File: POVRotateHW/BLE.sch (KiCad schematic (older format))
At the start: 3 parts

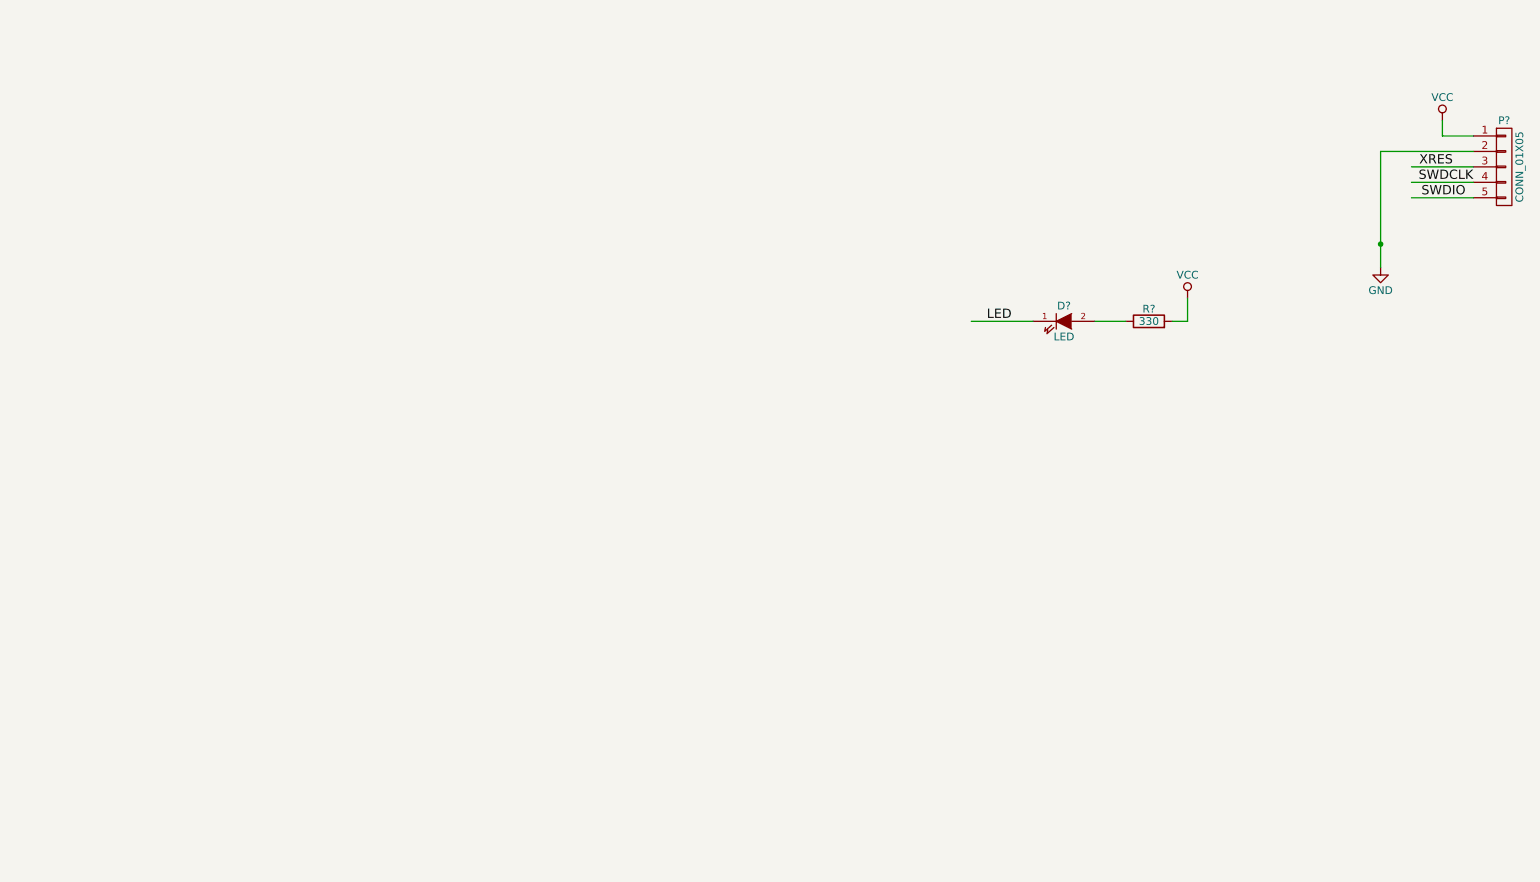
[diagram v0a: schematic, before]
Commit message: Started working on the schematic for the POV Rotate board.
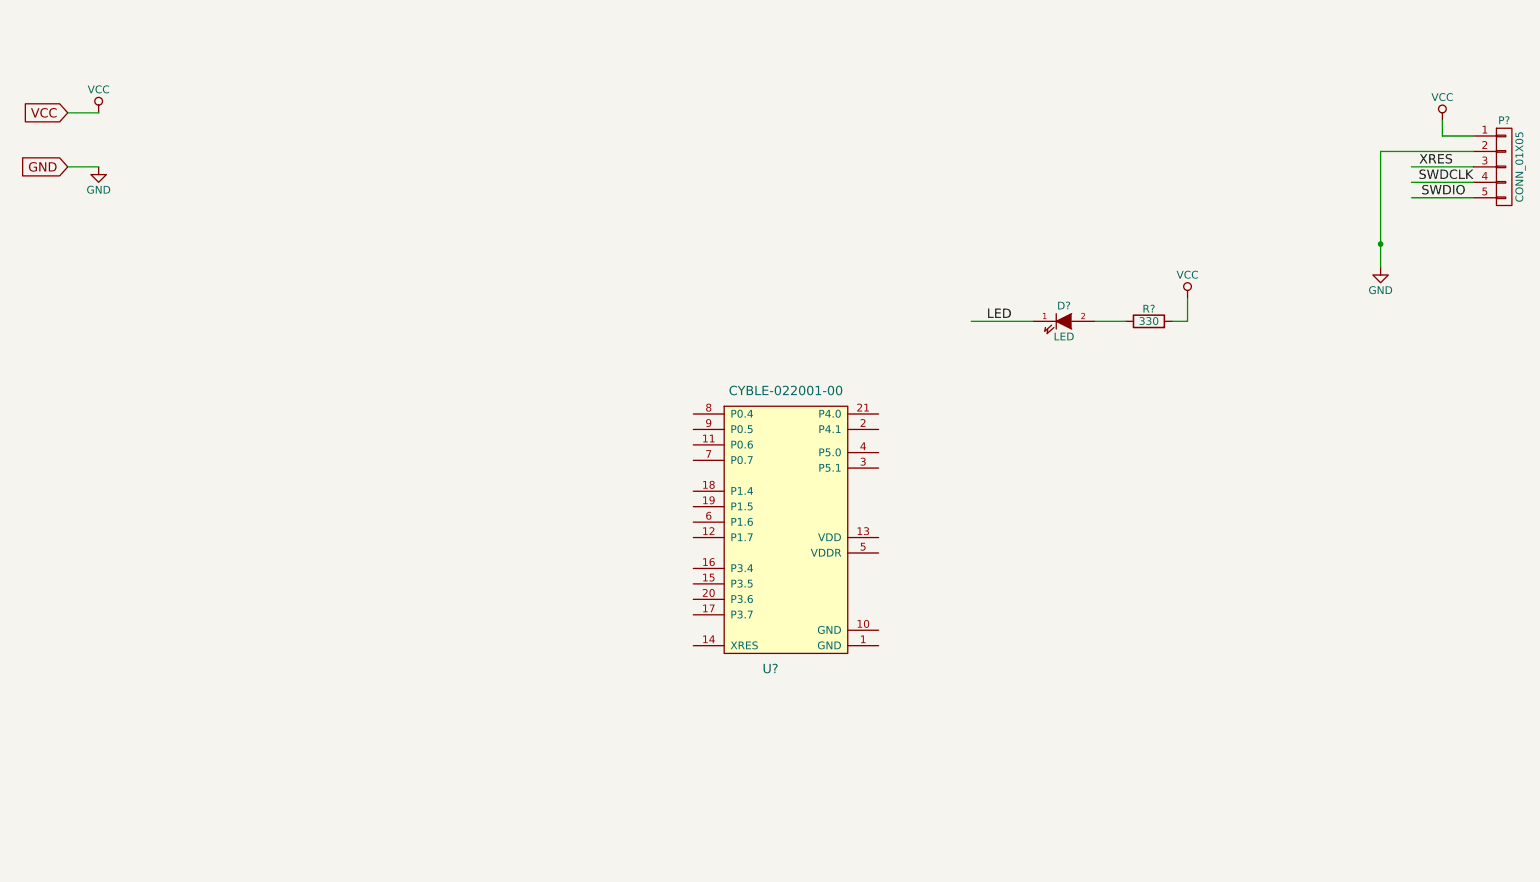
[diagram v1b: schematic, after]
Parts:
- added U?: CYBLE-022001-00, symbol CYBLE-022001-00
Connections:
- wire segments 11 -> 13
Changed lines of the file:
@@
 Text Label 10400 1700 2    60   ~ 0
 SWDIO
+$Comp
+L CYBLE-022001-00 U?
+U 1 1 5812CAAC
+P 6000 3750
+F 0 "U?" H 5900 2750 60  0000 C CNN
+F 1 "CYBLE-022001-00" H 6000 4550 60  0000 C CNN
+F 2 "" H 6000 4250 60  0001 C CNN
+F 3 "" H 6000 4250 60  0001 C CNN
+	1    6000 3750
+	1    0    0    -1
+$EndComp
+Text GLabel 1350 1150 0    60   Input ~ 0
+VCC
+Text GLabel 1350 1500 0    60   Input ~ 0
+GND
+$Comp
+L GND #PWR?
+U 1 1 581265FE
+P 1550 1500
+F 0 "#PWR?" H 1550 1250 50  0001 C CNN
+F 1 "GND" H 1550 1350 50  0000 C CNN
+F 2 "" H 1550 1500 50  0000 C CNN
+F 3 "" H 1550 1500 50  0000 C CNN
+	1    1550 1500
+	1    0    0    -1
+$EndComp
+$Comp
+L VCC #PWR?
+U 1 1 58126615
+P 1550 1150
+F 0 "#PWR?" H 1550 1000 50  0001 C CNN
+F 1 "VCC" H 1550 1300 50  0000 C CNN
+F 2 "" H 1550 1150 50  0000 C CNN
+F 3 "" H 1550 1150 50  0000 C CNN
+	1    1550 1150
+	1    0    0    -1
+$EndComp
+Wire Wire Line
+	1550 1500 1350 1500
+Wire Wire Line
+	1550 1150 1350 1150
 $EndSCHEMATC

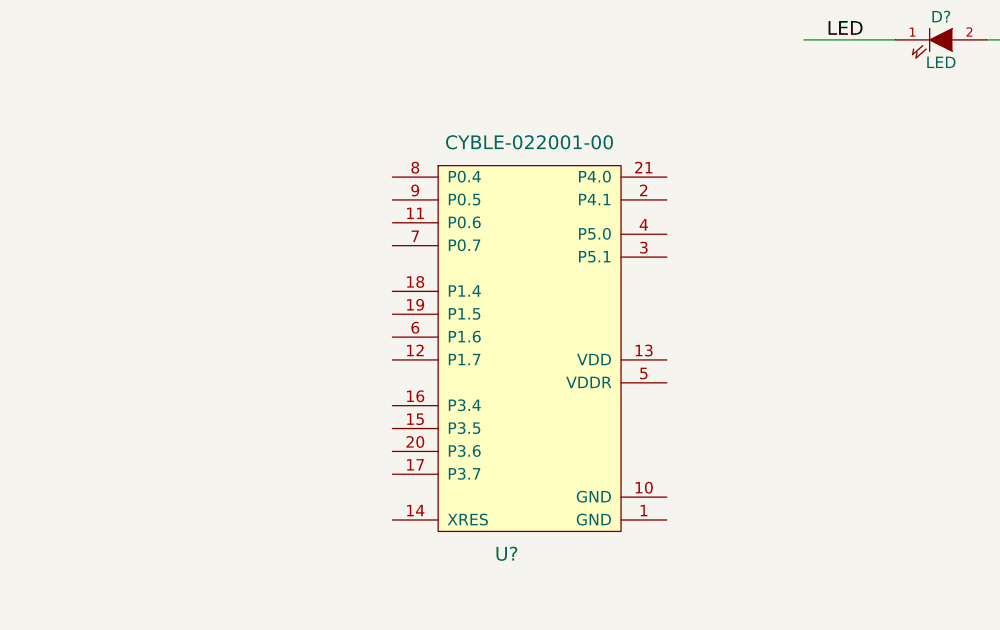
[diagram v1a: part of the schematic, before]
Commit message: Connected some pins up.
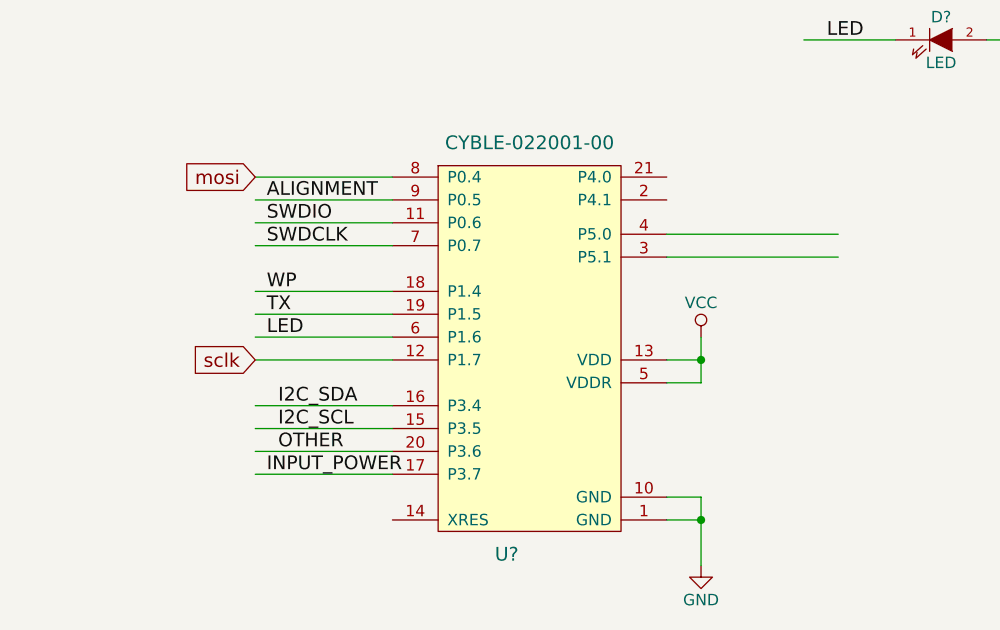
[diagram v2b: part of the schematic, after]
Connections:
- net labels added: ALIGNMENT, I2C_SCL, I2C_SDA, INPUT_POWER, OTHER, TX, WP, mosi, sclk
- wire segments 13 -> 33
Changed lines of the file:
@@
 	1    0    0    -1
 $EndComp
-Wire Wire Line
-	8500 2500 8600 2500
-Wire Wire Line
-	8600 2500 8600 2350
-Wire Wire Line
-	8000 2500 8200 2500
 $Comp
 L CONN_01X05 P?
@@
 	1    0    0    -1
 $EndComp
-Wire Wire Line
-	7600 2500 7200 2500
 Text Label 7300 2500 0    60   ~ 0
 LED
-Wire Wire Line
-	10250 1200 10250 1300
-Wire Wire Line
-	10250 1300 10450 1300
-Wire Wire Line
-	9850 1400 10450 1400
-Wire Wire Line
-	10450 1500 10050 1500
-Wire Wire Line
-	10450 1600 10050 1600
-Wire Wire Line
-	10450 1700 10050 1700
-Wire Wire Line
-	9850 1400 9850 2150
 Text Label 10100 1500 0    60   ~ 0
 XRES
-Connection ~ 9850 2000
 Text Label 10450 1600 2    60   ~ 0
 SWDCLK
@@
 	1    0    0    -1
 $EndComp
+Text GLabel 4800 3100 0    60   Input ~ 0
+mosi
+Text GLabel 4800 3900 0    60   Input ~ 0
+sclk
+Text Label 4850 3300 0    60   ~ 0
+SWDIO
+Text Label 4850 3400 0    60   ~ 0
+SWDCLK
+Text Label 4850 3800 0    60   ~ 0
+LED
+Text Label 4850 3200 0    60   ~ 0
+ALIGNMENT
+Text Label 4900 4200 0    60   ~ 0
+I2C_SCL
+Text Label 4900 4100 0    60   ~ 0
+I2C_SDA
+Text Label 4850 4400 0    60   ~ 0
+INPUT_POWER
+Text Label 4850 3600 0    60   ~ 0
+WP
+Text Label 4850 3700 0    60   ~ 0
+TX
+Text Label 4900 4300 0    60   ~ 0
+OTHER
+$Comp
+L VCC #PWR?
+U 1 1 5814CF5A
+P 6750 3800
+F 0 "#PWR?" H 6750 3650 50  0001 C CNN
+F 1 "VCC" H 6750 3950 50  0000 C CNN
+F 2 "" H 6750 3800 50  0000 C CNN
+F 3 "" H 6750 3800 50  0000 C CNN
+	1    6750 3800
+	1    0    0    -1
+$EndComp
+$Comp
+L GND #PWR?
+U 1 1 5814CF60
+P 6750 4800
+F 0 "#PWR?" H 6750 4550 50  0001 C CNN
+F 1 "GND" H 6750 4650 50  0000 C CNN
+F 2 "" H 6750 4800 50  0000 C CNN
+F 3 "" H 6750 4800 50  0000 C CNN
+	1    6750 4800
+	1    0    0    -1
+$EndComp
+Wire Wire Line
+	8500 2500 8600 2500
+Wire Wire Line
+	8600 2500 8600 2350
+Wire Wire Line
+	8000 2500 8200 2500
+Wire Wire Line
+	7600 2500 7200 2500
+Wire Wire Line
+	10250 1200 10250 1300
+Wire Wire Line
+	10250 1300 10450 1300
+Wire Wire Line
+	9850 1400 10450 1400
+Wire Wire Line
+	10450 1500 10050 1500
+Wire Wire Line
+	10450 1600 10050 1600
+Wire Wire Line
+	10450 1700 10050 1700
+Wire Wire Line
+	9850 1400 9850 2150
+Connection ~ 9850 2000
 Wire Wire Line
 	1550 1500 1350 1500
 Wire Wire Line
 	1550 1150 1350 1150
+Wire Wire Line
+	4800 3100 5400 3100
+Wire Wire Line
+	5400 3900 4800 3900
+Wire Wire Line
+	6600 3350 7350 3350
+Wire Wire Line
+	6600 3450 7350 3450
+Wire Wire Line
+	5400 3400 4800 3400
+Wire Wire Line
+	5400 3300 4800 3300
+Wire Wire Line
+	5400 3800 4800 3800
+Wire Wire Line
+	5400 3200 4800 3200
+Wire Wire Line
+	5400 4200 4800 4200
+Wire Wire Line
+	5400 4100 4800 4100
+Wire Wire Line
+	5400 4400 4800 4400
+Wire Wire Line
+	5400 3600 4800 3600
+Wire Wire Line
+	5400 3700 4800 3700
+Wire Wire Line
+	5400 4300 4800 4300
+Wire Wire Line
+	6600 3900 6750 3900
+Wire Wire Line
+	6750 3800 6750 4000
+Wire Wire Line
+	6750 4000 6600 4000
+Connection ~ 6750 3900
+Wire Wire Line
+	6600 4600 6750 4600
+Wire Wire Line
+	6750 4500 6750 4800
+Wire Wire Line
+	6600 4500 6750 4500
+Connection ~ 6750 4600
 $EndSCHEMATC

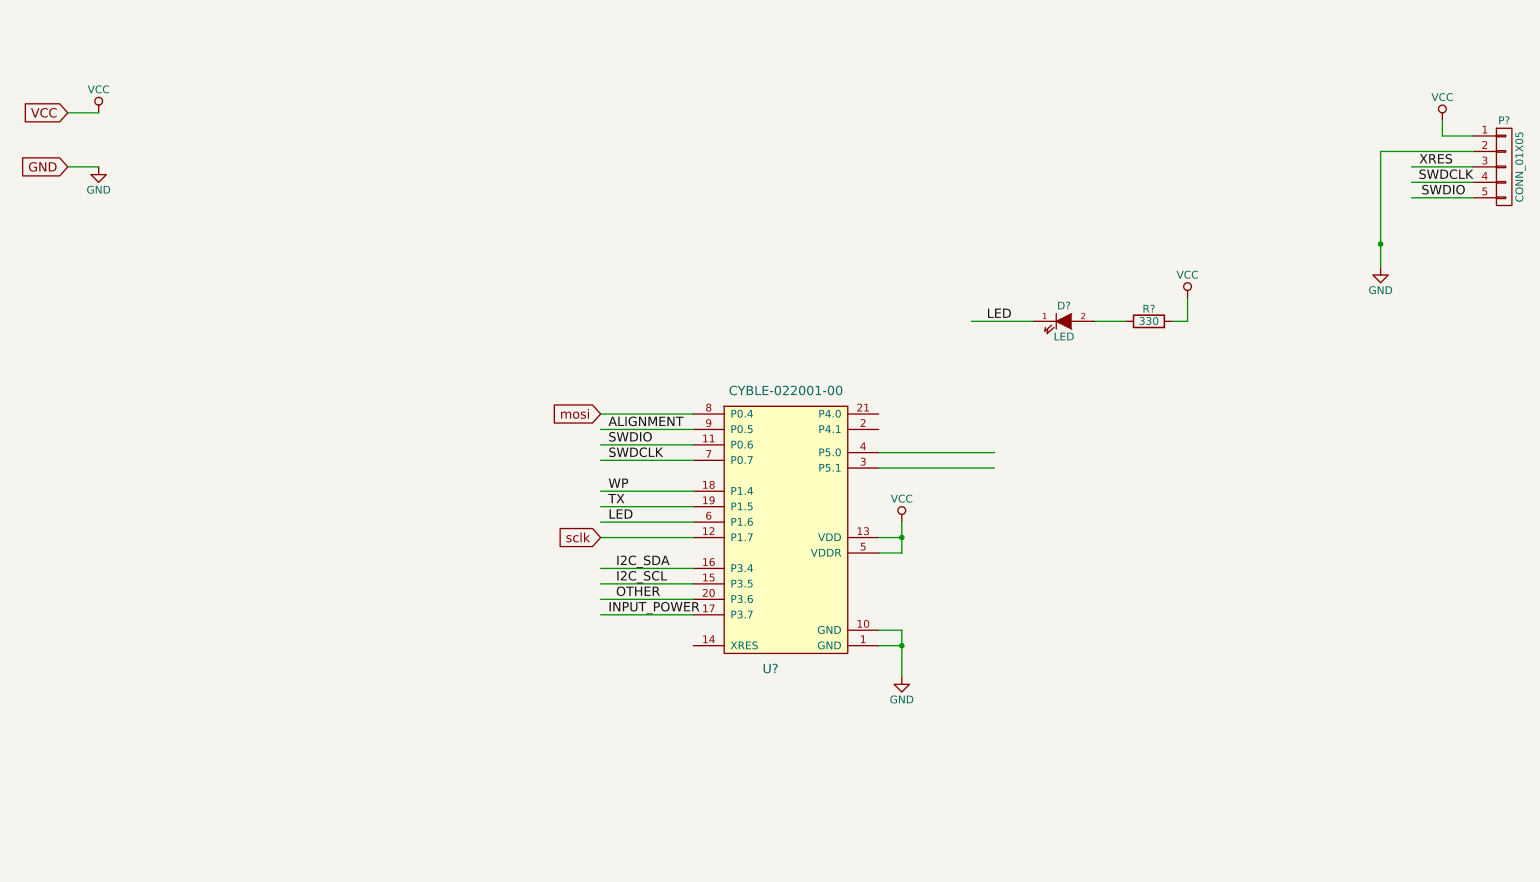
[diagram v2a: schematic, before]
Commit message: Finished the schematic for the POVRotate system, started on layout.
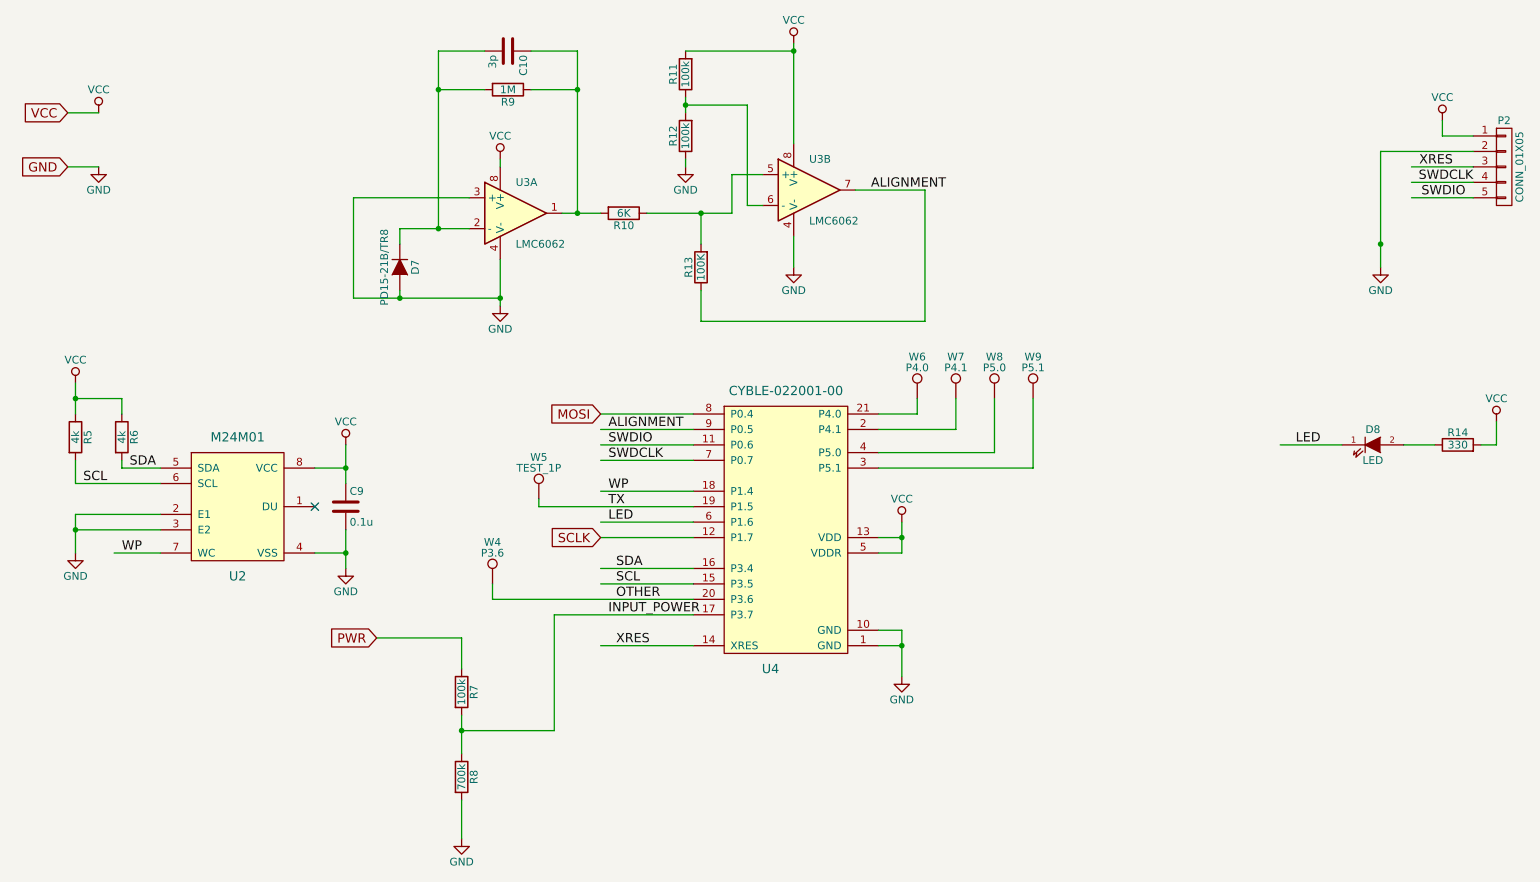
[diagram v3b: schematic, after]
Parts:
- added C10: 3p, symbol C
- added C9: 0.1u, symbol C
- added D7: PD15-21B/TR8, symbol D
- added R10: 6K, symbol R
- added R11, R12, R7: 100k, symbol R
- added R13: 100K, symbol R
- added R5, R6: 4k, symbol R
- added R8: 700k, symbol R
- added R9: 1M, symbol R
- added U2: M24M01, symbol M24M01
- added U3: LMC6062, symbol LMC6062
- added W4: P3.6, symbol TEST_1P
- added W5: TEST_1P, symbol TEST_1P
- added W6: P4.0, symbol TEST_1P
- added W7: P4.1, symbol TEST_1P
- added W8: P5.0, symbol TEST_1P
- added W9: P5.1, symbol TEST_1P
- U4: renamed from U?; DIGIKEY (none) -> 428-3566-PROMO-ND
- gave numbers to parts that had none: 3
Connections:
- net labels added: MOSI, PWR, SCL, SCLK, SDA
- net labels removed: I2C_SCL, I2C_SDA, mosi, sclk
- wire segments 33 -> 94
- no-connect marks 0 -> 1
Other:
- moved on the sheet: D8, R14
